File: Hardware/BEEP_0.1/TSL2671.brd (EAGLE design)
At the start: 22.6 x 29.9 mm, 10 parts, among them IC1 TSL2671

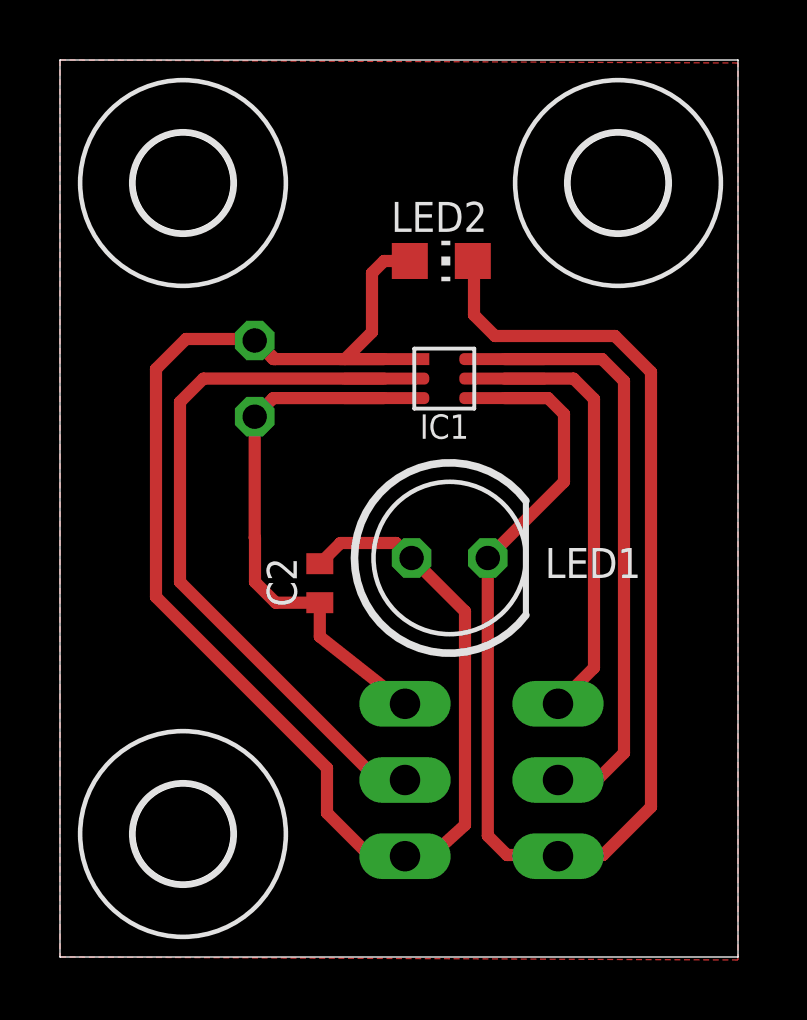
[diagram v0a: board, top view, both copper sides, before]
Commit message: enlarge Clearence to 10mil created some pdf files for the boards
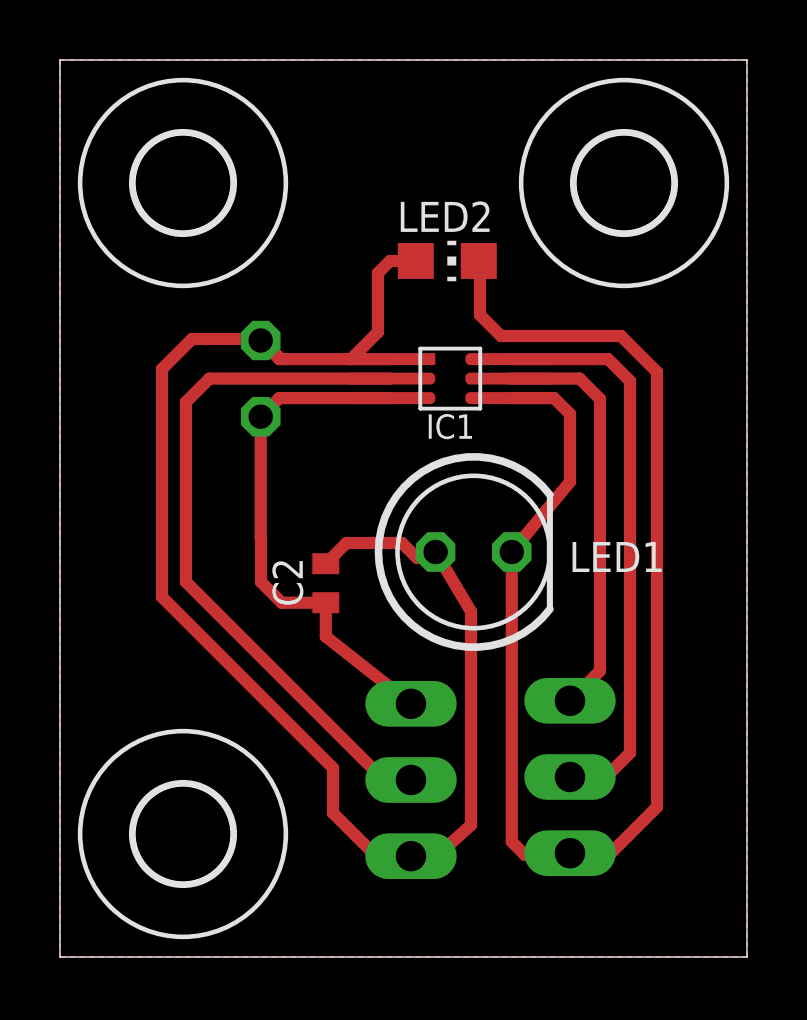
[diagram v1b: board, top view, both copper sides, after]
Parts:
- moved LED1 0.82 mm to (13.8, 13.5)
- moved JP3 0.41 mm to (17.0, 6.00)
- moved C1 0.20 mm to (6.69, 19.3)
- moved C2 0.20 mm to (8.86, 12.5)
- moved IC1 0.20 mm to (13.0, 19.3)
- moved JP2 0.20 mm to (11.7, 5.90)
- moved LED2 0.20 mm to (12.9, 23.2)
- moved U$4 0.20 mm to (18.8, 25.8)
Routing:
- net N$1: track 46.7 -> 46.2 mm
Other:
- board size 22.6 x 29.9 mm -> 22.9 x 29.9 mm

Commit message: Add branding ;) enhance PCBs finish Easy RGB Board add Texas Instruments libray from Element 14 add dxf import ulp for eagle add Script for easy eagle export to pdf for etching minor cleanup
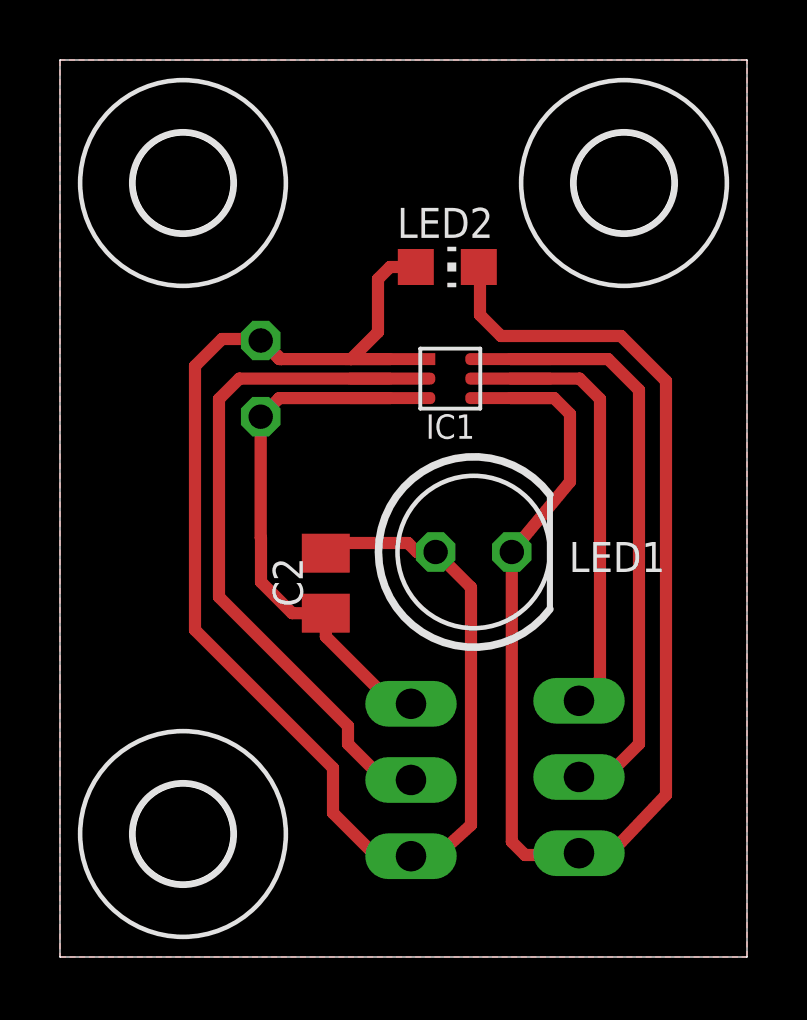
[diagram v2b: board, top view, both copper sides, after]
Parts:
- added U$1: LOGO-COPPER4, Branding:COPPER4
- C2: device rcl:C1005 -> rcl:C0805K
- moved JP3 0.30 mm to (17.3, 6.00)
- moved LED2 0.20 mm to (12.9, 23.0)
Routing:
- net VCC: track 51.4 -> 49.5 mm
- net N$2: track 23.4 -> 21.9 mm
- net N$1: track 46.2 -> 47.1 mm
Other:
- board text added: "TSL2671 v0.1.1"

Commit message: remove GND under TSL2671 fix LED size fix Cap size
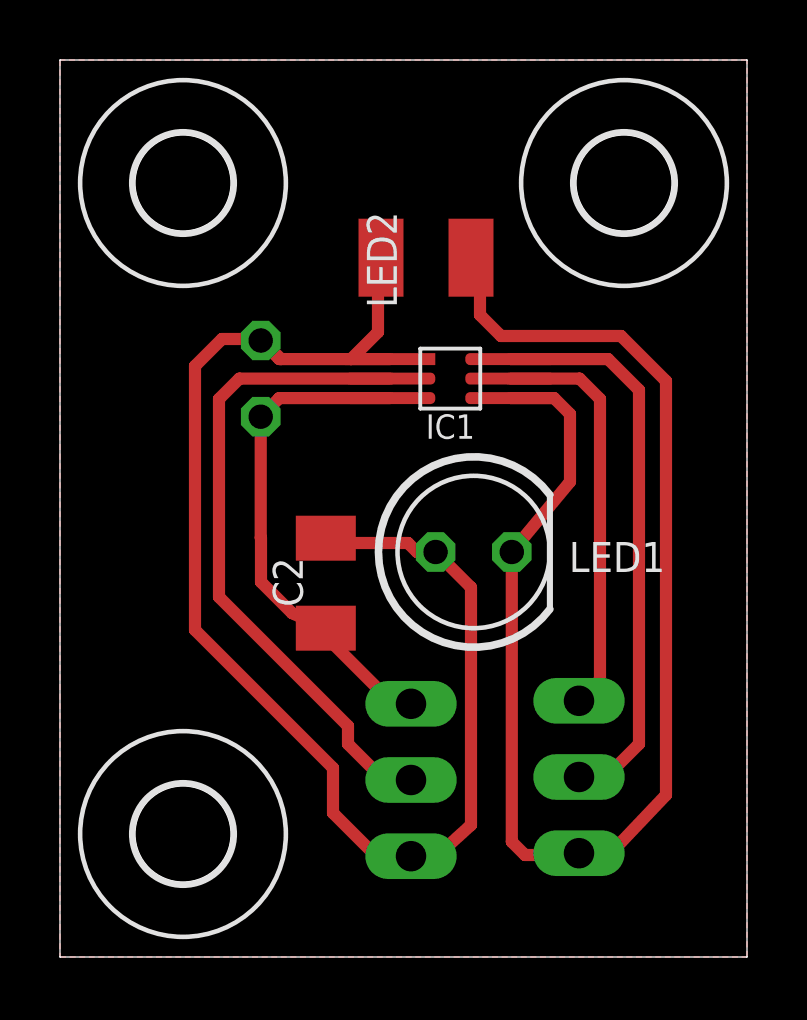
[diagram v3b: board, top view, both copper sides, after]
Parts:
- C2: device rcl:C0805K -> rcl:C1206K
- LED2: value (none) -> GM5BW96385A; device led:CHIP-LED0805 -> led:GM5BW96385A
- moved LED2 0.77 mm to (12.2, 23.3), turned to 0 degrees
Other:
- board text added: "TSL2671 v0.2"
- board text removed: "TSL2671 v0.1.1"
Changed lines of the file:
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@@
 <layers>
 <layer number="1" name="Top" color="4" fill="1" visible="yes" active="yes"/>
-<layer number="16" name="Bottom" color="1" fill="1" visible="yes" active="yes"/>
+<layer number="16" name="Bottom" color="1" fill="1" visible="no" active="yes"/>
 <layer number="17" name="Pads" color="2" fill="1" visible="yes" active="yes"/>
 <layer number="18" name="Vias" color="2" fill="1" visible="yes" active="yes"/>
-<layer number="19" name="Unrouted" color="6" fill="1" visible="yes" active="yes"/>
-<layer number="20" name="Dimension" color="15" fill="1" visible="yes" active="yes"/>
-<layer number="21" name="tPlace" color="7" fill="1" visible="yes" active="yes"/>
-<layer number="22" name="bPlace" color="7" fill="1" visible="yes" active="yes"/>
-<layer number="23" name="tOrigins" color="15" fill="1" visible="yes" active="yes"/>
-<layer number="24" name="bOrigins" color="15" fill="1" visible="yes" active="yes"/>
-<layer number="25" name="tNames" color="7" fill="1" visible="yes" active="yes"/>
-<layer number="26" name="bNames" color="7" fill="1" visible="yes" active="yes"/>
-<layer number="27" name="tValues" color="7" fill="1" visible="yes" active="yes"/>
-<layer number="28" name="bValues" color="7" fill="1" visible="yes" active="yes"/>
+<layer number="19" name="Unrouted" color="6" fill="1" visible="no" active="yes"/>
+<layer number="20" name="Dimension" color="15" fill="1" visible="no" active="yes"/>
+<layer number="21" name="tPlace" color="7" fill="1" visible="no" active="yes"/>
+<layer number="22" name="bPlace" color="7" fill="1" visible="no" active="yes"/>
+<layer number="23" name="tOrigins" color="15" fill="1" visible="no" active="yes"/>
+<layer number="24" name="bOrigins" color="15" fill="1" visible="no" active="yes"/>
+<layer number="25" name="tNames" color="7" fill="1" visible="no" active="yes"/>
+<layer number="26" name="bNames" color="7" fill="1" visible="no" active="yes"/>
+<layer number="27" name="tValues" color="7" fill="1" visible="no" active="yes"/>
+<layer number="28" name="bValues" color="7" fill="1" visible="no" active="yes"/>
 <layer number="29" name="tStop" color="7" fill="3" visible="no" active="yes"/>
 <layer number="30" name="bStop" color="7" fill="6" visible="no" active="yes"/>
@@
 <layer number="37" name="tTest" color="7" fill="1" visible="no" active="yes"/>
 <layer number="38" name="bTest" color="7" fill="1" visible="no" active="yes"/>
-<layer number="39" name="tKeepout" color="4" fill="11" visible="yes" active="yes"/>
-<layer number="40" name="bKeepout" color="1" fill="11" visible="yes" active="yes"/>
-<layer number="41" name="tRestrict" color="4" fill="10" visible="yes" active="yes"/>
-<layer number="42" name="bRestrict" color="1" fill="10" visible="yes" active="yes"/>
-<layer number="43" name="vRestrict" color="2" fill="10" visible="yes" active="yes"/>
+<layer number="39" name="tKeepout" color="4" fill="11" visible="no" active="yes"/>
+<layer number="40" name="bKeepout" color="1" fill="11" visible="no" active="yes"/>
+<layer number="41" name="tRestrict" color="4" fill="10" visible="no" active="yes"/>
+<layer number="42" name="bRestrict" color="1" fill="10" visible="no" active="yes"/>
+<layer number="43" name="vRestrict" color="2" fill="10" visible="no" active="yes"/>
 <layer number="44" name="Drills" color="7" fill="1" visible="no" active="yes"/>
 <layer number="45" name="Holes" color="7" fill="1" visible="yes" active="yes"/>
@@
 <layer number="48" name="Document" color="7" fill="1" visible="no" active="yes"/>
 <layer number="49" name="Reference" color="7" fill="1" visible="no" active="yes"/>
-<layer number="51" name="tDocu" color="7" fill="1" visible="yes" active="yes"/>
-<layer number="52" name="bDocu" color="7" fill="1" visible="yes" active="yes"/>
+<layer number="51" name="tDocu" color="7" fill="1" visible="no" active="yes"/>
+<layer number="52" name="bDocu" color="7" fill="1" visible="no" active="yes"/>
 <layer number="91" name="Nets" color="2" fill="1" visible="no" active="no"/>
 <layer number="92" name="Busses" color="1" fill="1" visible="no" active="no"/>
@@
 <layer number="98" name="Guide" color="6" fill="1" visible="no" active="no"/>
 <layer number="100" name="tCName" color="7" fill="1" visible="yes" active="yes"/>
-<layer number="101" name="bCName" color="7" fill="1" visible="yes" active="yes"/>
+<layer number="101" name="bCName" color="7" fill="1" visible="no" active="yes"/>
 </layers>
 <board>
@@
 <text x="18.5" y="6.5" size="1" layer="26" rot="MR135" align="center-left">SDA</text>
 <text x="3.3" y="15.6" size="1.016" layer="100" rot="R90">TSL2671
-v0.1.1</text>
+v0.2</text>
 <polygon width="0.4064" layer="41">
 <vertex x="0" y="21.2"/>
@@
 <vertex x="0" y="8.6"/>
 </polygon>
+<wire x1="12.9" y1="20.5" x2="12.9" y2="17.9" width="0.4064" layer="41"/>
+<wire x1="12" y1="17.9" x2="15.8" y2="17.9" width="0.4064" layer="41"/>
+<wire x1="11.9" y1="17.9" x2="9.8" y2="17.9" width="0.4064" layer="41"/>
+<wire x1="12.2" y1="21.7" x2="12.2" y2="24.5" width="0.4064" layer="41"/>
 </plain>
 <attributes>
@@
 <attribute name="VALUE" x="16.9904" y="11.6966" size="1.27" layer="27" ratio="10"/>
 </element>
-<element name="LED2" library="led" package="CHIP-LED0805" value="" x="12.91" y="23" smashed="yes" rot="R270">
-<attribute name="NAME" x="12.84" y="24.47" size="1" layer="25" align="center"/>
-<attribute name="VALUE" x="11.64" y="20.46" size="1.27" layer="27"/>
+<element name="LED2" library="led" package="GM5BW96385A" value="GM5BW96385A" x="12.2" y="23.31" smashed="yes">
+<attribute name="NAME" x="10.73" y="23.24" size="1" layer="25" rot="R90" align="center"/>
+<attribute name="VALUE" x="14.74" y="22.04" size="1.27" layer="27" rot="R90"/>
 </element>
 <element name="C1" library="rcl" package="C025-025X050" value="1uf" x="6.69" y="19.28" smashed="yes" rot="MR270">
@@
 <attribute name="VALUE" x="9.284" y="20.466" size="1" layer="28" ratio="10" rot="MR270"/>
 </element>
-<element name="C2" library="rcl" package="C0805K" value="1uf" x="8.86" y="12.46" smashed="yes" rot="R270">
+<element name="C2" library="rcl" package="C1206K" value="1uf" x="8.86" y="12.46" smashed="yes" rot="R270">
 <attribute name="NAME" x="7.595" y="12.495" size="1" layer="25" rot="R90" align="center"/>
 <attribute name="VALUE" x="8.755" y="14.195" size="1" layer="27" rot="R90" align="center-left"/>
@@
 <wire x1="11.01" y1="19.93" x2="9.7" y2="19.93" width="0.4064" layer="1"/>
 <wire x1="7.37" y1="19.93" x2="7.31" y2="19.93" width="0.4064" layer="1"/>
-<wire x1="11.86" y1="23" x2="11" y2="23" width="0.4064" layer="1"/>
+<wire x1="10.7" y1="23.31" x2="11" y2="23" width="0.4064" layer="1"/>
 <wire x1="11" y1="23" x2="10.6" y2="22.6" width="0.4064" layer="1"/>
 <wire x1="10.6" y1="22.6" x2="10.6" y2="20.83" width="0.4064" layer="1"/>
@@
 <wire x1="11.9" y1="13.5" x2="11.6" y2="13.8" width="0.4064" layer="1"/>
 <wire x1="11.6" y1="13.8" x2="9.55" y2="13.8" width="0.4064" layer="1"/>
-<wire x1="9.55" y1="13.8" x2="8.86" y2="13.46" width="0.4064" layer="1"/>
+<wire x1="9.55" y1="13.8" x2="8.86" y2="13.96" width="0.4064" layer="1"/>
 </signal>
 <signal name="N$1">
@@
 <wire x1="14.7" y1="20.7" x2="14" y2="21.4" width="0.4064" layer="1"/>
 <wire x1="14" y1="21.4" x2="14" y2="23.16" width="0.4064" layer="1"/>
-<wire x1="14" y1="23.16" x2="13.96" y2="23" width="0.4064" layer="1"/>
+<wire x1="14" y1="23.16" x2="13.7" y2="23.31" width="0.4064" layer="1"/>
 </signal>
 <signal name="GND">
@@
 <wire x1="11.01" y1="18.63" x2="7.31" y2="18.63" width="0.4064" layer="1"/>
 <wire x1="7.31" y1="18.63" x2="6.69" y2="18.01" width="0.4064" layer="1"/>
-<wire x1="8.86" y1="11.46" x2="8.86" y2="10.68" width="0.4064" layer="1"/>
+<wire x1="8.86" y1="10.96" x2="8.86" y2="10.68" width="0.4064" layer="1"/>
 <wire x1="6.7" y1="12.5" x2="6.7" y2="13.97" width="0.4064" layer="1"/>
 <wire x1="6.7" y1="13.97" x2="6.69" y2="13.98" width="0.4064" layer="1"/>
@@
 </polygon>
 <wire x1="6.69" y1="18.01" x2="6.69" y2="13.98" width="0.4064" layer="1"/>
-<wire x1="8.86" y1="11.46" x2="7.74" y2="11.46" width="0.4064" layer="1"/>
+<wire x1="8.86" y1="10.96" x2="7.74" y2="11.46" width="0.4064" layer="1"/>
 <wire x1="7.74" y1="11.46" x2="6.7" y2="12.5" width="0.4064" layer="1"/>
 <wire x1="11.7" y1="8.44" x2="11.1" y2="8.44" width="0.4064" layer="1"/>
